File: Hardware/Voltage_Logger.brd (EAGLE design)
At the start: 48.3 x 27.1 mm, 59 parts, among them IC1 NCP1117ST33T3G, Q1 ABLS2-8.000MHZ, U1 STM32F405RGT6, X2 22-23-2021

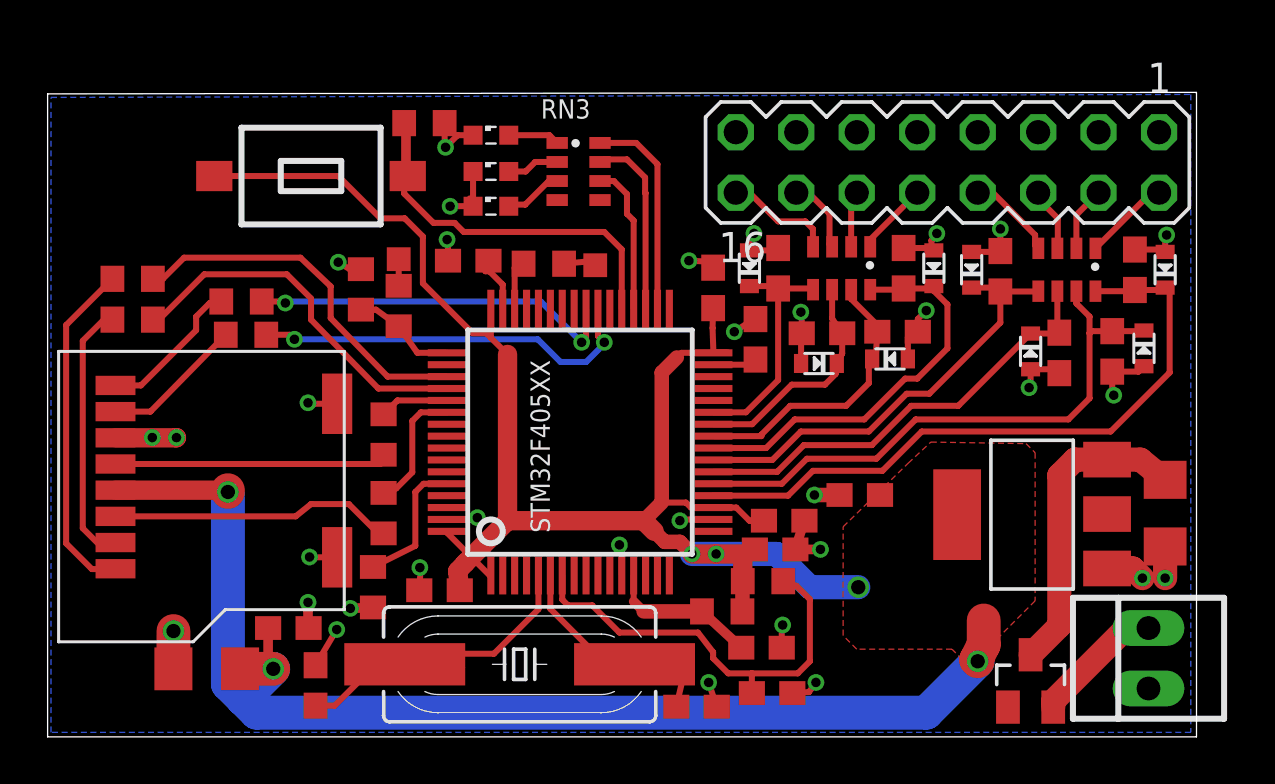
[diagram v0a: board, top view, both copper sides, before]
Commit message: channels remapped, documentation added, ready for tindie
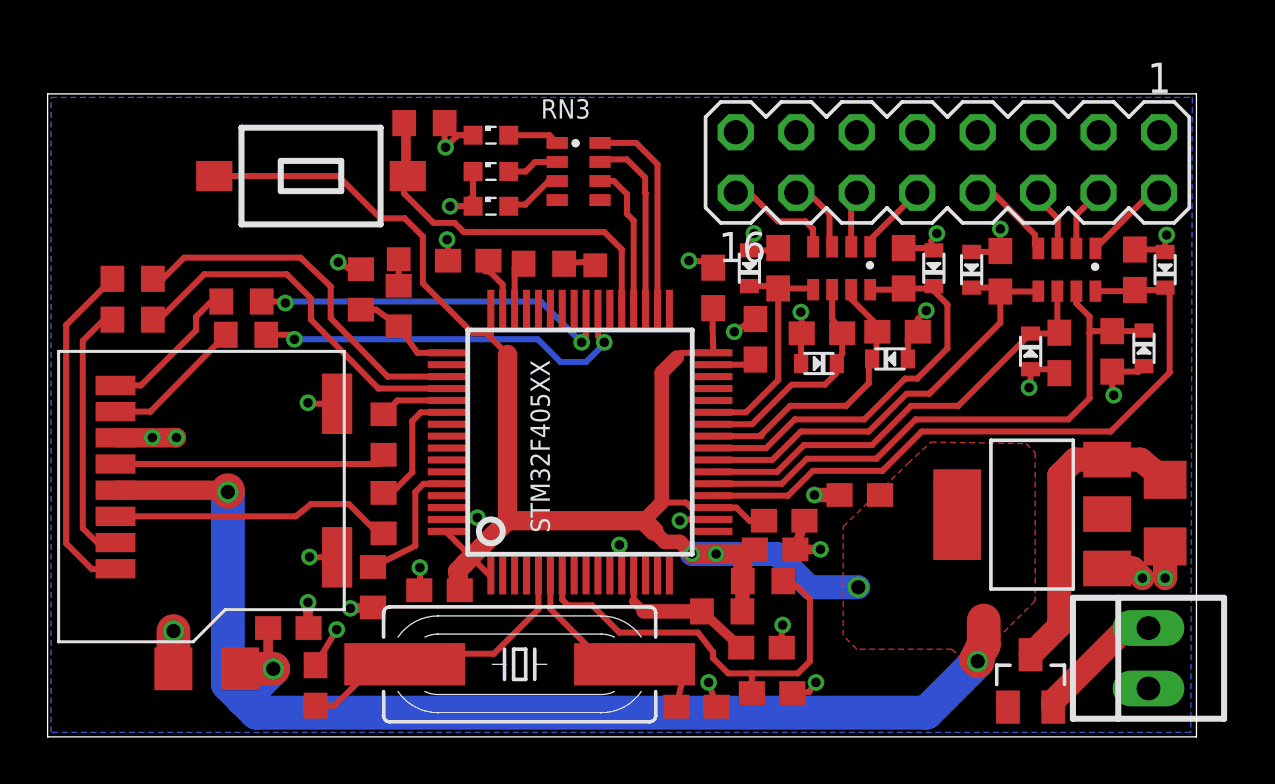
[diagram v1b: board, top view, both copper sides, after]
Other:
- board size 48.3 x 27.1 mm -> 48.3 x 27 mm
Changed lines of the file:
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@@
 <plain>
 <wire x1="-0.905" y1="-5.3975" x2="47.3535" y2="-5.3975" width="0" layer="20"/>
-<wire x1="47.3535" y1="-5.3975" x2="47.3535" y2="21.675" width="0" layer="20"/>
-<wire x1="47.3535" y1="21.675" x2="-0.905" y2="21.6115" width="0" layer="20"/>
+<wire x1="47.3535" y1="-5.3975" x2="47.3535" y2="21.6115" width="0" layer="20"/>
+<wire x1="47.3535" y1="21.6115" x2="-0.905" y2="21.6115" width="0" layer="20"/>
 <wire x1="-0.905" y1="21.6115" x2="-0.905" y2="-5.3975" width="0" layer="20"/>
 </plain>
@@
 <vertex x="-0.762" y="-5.207"/>
 <vertex x="-0.762" y="21.463"/>
-<vertex x="47.117" y="21.59"/>
+<vertex x="47.1805" y="21.463"/>
 <vertex x="47.117" y="-5.207"/>
 </polygon>
